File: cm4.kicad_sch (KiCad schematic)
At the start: 54 parts, among them Q1 MMBT2222AM3T5G, U3 PCA9671BS,118, U4 SN74LVC1G04DRY, U5 SN74LVC1G07DRY

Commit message: footprint assignment
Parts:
- R26, R27, R28, R29: renamed from R?; footprint (none) -> Resistor_SMD:R_0402_1005Metric
- gave numbers to parts that had none: 5
- renumbered R8 to R10, R9 to R11, R10 to R12, R11 to R13, R12 to R14, R13 to R15, R14 to R16, R15 to R17, R16 to R18, R17 to R19, R18 to R20, R19 to R21, R20 to R22, R21 to R23, R22 to R24, R23 to R25, R7 to R9
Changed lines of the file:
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@@
   (symbol (lib_id "Device:R_Small") (at 499.11 342.9 90) (unit 1)
     (in_bom yes) (on_board yes)
-    (property "Reference" "R15" (id 0) (at 496.57 341.63 90)
+    (property "Reference" "R17" (id 0) (at 496.57 341.63 90)
       (effects (font (size 1.27 1.27)) (justify left))
     )
@@
   (symbol (lib_id "Device:R_Small") (at 647.7 118.11 90) (unit 1)
     (in_bom yes) (on_board yes)
-    (property "Reference" "R?" (id 0) (at 645.16 116.84 90)
+    (property "Reference" "R29" (id 0) (at 645.16 116.84 90)
       (effects (font (size 1.27 1.27)) (justify left))
     )
@@
       (effects (font (size 1.27 1.27)) (justify right))
     )
-    (property "Footprint" "" (id 2) (at 647.7 118.11 0)
+    (property "Footprint" "Resistor_SMD:R_0402_1005Metric" (id 2) (at 647.7 118.11 0)
       (effects (font (size 1.27 1.27)) hide)
     )
@@
   (symbol (lib_id "Device:R_Small") (at 458.47 129.54 90) (unit 1)
     (in_bom yes) (on_board yes)
-    (property "Reference" "R9" (id 0) (at 453.39 128.27 90))
+    (property "Reference" "R11" (id 0) (at 453.39 128.27 90))
     (property "Value" "1k" (id 1) (at 463.55 128.27 90))
     (property "Footprint" "Resistor_SMD:R_0402_1005Metric" (id 2) (at 458.47 129.54 0)
@@
   (symbol (lib_id "Device:R_Small") (at 499.11 322.58 270) (mirror x) (unit 1)
     (in_bom yes) (on_board yes)
-    (property "Reference" "R13" (id 0) (at 496.57 321.31 90)
+    (property "Reference" "R15" (id 0) (at 496.57 321.31 90)
       (effects (font (size 1.27 1.27)) (justify right))
     )
@@
   (symbol (lib_id "Device:C_Small") (at 607.06 69.85 0) (unit 1)
     (in_bom yes) (on_board yes)
-    (property "Reference" "C?" (id 0) (at 608.965 68.58 0)
+    (property "Reference" "C9" (id 0) (at 608.965 68.58 0)
       (effects (font (size 1.27 1.27)) (justify left))
     )
@@
   (symbol (lib_id "Interface_I2C_NXP:PCA9641BSHP") (at 623.57 62.23 0) (unit 1)
     (in_bom yes) (on_board yes) (fields_autoplaced)
-    (property "Reference" "U?" (id 0) (at 670.56 53.34 0))
+    (property "Reference" "U6" (id 0) (at 670.56 53.34 0))
     (property "Value" "PCA9641BSHP" (id 1) (at 670.56 55.88 0))
     (property "Footprint" "Interface_I2C_NXP:SOT758-1_HVQFN-16_3x3mm_P0.5mm_EP1.75x1.75mm_NXP" (id 2) (at 670.56 142.24 0)
@@
   (symbol (lib_id "Device:R_Small") (at 500.38 97.79 180) (unit 1)
     (in_bom yes) (on_board yes)
-    (property "Reference" "R17" (id 0) (at 501.65 96.52 0)
+    (property "Reference" "R19" (id 0) (at 501.65 96.52 0)
       (effects (font (size 1.27 1.27)) (justify right))
     )
@@
   (symbol (lib_id "Device:R_Small") (at 414.02 383.54 270) (mirror x) (unit 1)
     (in_bom yes) (on_board yes)
-    (property "Reference" "R?" (id 0) (at 414.02 379.095 90))
+    (property "Reference" "R8" (id 0) (at 414.02 379.095 90))
     (property "Value" "5.1k" (id 1) (at 414.02 381 90))
     (property "Footprint" "Resistor_SMD:R_0402_1005Metric" (id 2) (at 414.02 383.54 0)
@@
   (symbol (lib_id "Device:R_Small") (at 554.99 203.2 90) (unit 1)
     (in_bom yes) (on_board yes)
-    (property "Reference" "R23" (id 0) (at 557.53 201.93 90)
+    (property "Reference" "R25" (id 0) (at 557.53 201.93 90)
       (effects (font (size 1.27 1.27)) (justify right))
     )
@@
   (symbol (lib_id "Device:R_Small") (at 647.7 110.49 90) (unit 1)
     (in_bom yes) (on_board yes)
-    (property "Reference" "R?" (id 0) (at 645.16 109.22 90)
+    (property "Reference" "R26" (id 0) (at 645.16 109.22 90)
       (effects (font (size 1.27 1.27)) (justify left))
     )
@@
       (effects (font (size 1.27 1.27)) (justify right))
     )
-    (property "Footprint" "" (id 2) (at 647.7 110.49 0)
+    (property "Footprint" "Resistor_SMD:R_0402_1005Metric" (id 2) (at 647.7 110.49 0)
       (effects (font (size 1.27 1.27)) hide)
     )
@@
   (symbol (lib_id "Device:R_Small") (at 504.19 191.77 0) (unit 1)
     (in_bom yes) (on_board yes)
-    (property "Reference" "R18" (id 0) (at 505.46 190.5 0)
+    (property "Reference" "R20" (id 0) (at 505.46 190.5 0)
       (effects (font (size 1.27 1.27)) (justify left))
     )
@@
   (symbol (lib_id "power:GND") (at 626.11 140.97 0) (unit 1)
     (in_bom yes) (on_board yes) (fields_autoplaced)
-    (property "Reference" "#PWR?" (id 0) (at 626.11 147.32 0)
+    (property "Reference" "#PWR016" (id 0) (at 626.11 147.32 0)
       (effects (font (size 1.27 1.27)) hide)
     )
@@
   (symbol (lib_id "Device:C_Small") (at 619.76 69.85 0) (unit 1)
     (in_bom yes) (on_board yes)
-    (property "Reference" "C?" (id 0) (at 621.665 68.58 0)
+    (property "Reference" "C10" (id 0) (at 621.665 68.58 0)
       (effects (font (size 1.27 1.27)) (justify left))
     )
@@
   (symbol (lib_id "Device:R_Small") (at 458.47 124.46 90) (unit 1)
     (in_bom yes) (on_board yes)
-    (property "Reference" "R7" (id 0) (at 453.39 123.19 90))
+    (property "Reference" "R9" (id 0) (at 453.39 123.19 90))
     (property "Value" "1k" (id 1) (at 463.55 123.19 90))
     (property "Footprint" "Resistor_SMD:R_0402_1005Metric" (id 2) (at 458.47 124.46 0)
@@
   (symbol (lib_id "Device:R_Small") (at 491.49 217.17 90) (unit 1)
     (in_bom yes) (on_board yes)
-    (property "Reference" "R11" (id 0) (at 491.49 212.09 90))
+    (property "Reference" "R13" (id 0) (at 491.49 212.09 90))
     (property "Value" "5.9k" (id 1) (at 491.49 214.63 90))
     (property "Footprint" "Resistor_SMD:R_0402_1005Metric" (id 2) (at 491.49 217.17 0)
@@
   (symbol (lib_id "Device:R_Small") (at 506.73 97.79 180) (unit 1)
     (in_bom yes) (on_board yes)
-    (property "Reference" "R19" (id 0) (at 508 96.52 0)
+    (property "Reference" "R21" (id 0) (at 508 96.52 0)
       (effects (font (size 1.27 1.27)) (justify right))
     )
@@
   (symbol (lib_id "Device:R_Small") (at 510.54 256.54 270) (mirror x) (unit 1)
     (in_bom yes) (on_board yes)
-    (property "Reference" "R20" (id 0) (at 508 255.27 90)
+    (property "Reference" "R22" (id 0) (at 508 255.27 90)
       (effects (font (size 1.27 1.27)) (justify right))
     )
@@
   (symbol (lib_id "Device:R_Small") (at 647.7 115.57 90) (unit 1)
     (in_bom yes) (on_board yes)
-    (property "Reference" "R?" (id 0) (at 645.16 114.3 90)
+    (property "Reference" "R28" (id 0) (at 645.16 114.3 90)
       (effects (font (size 1.27 1.27)) (justify left))
     )
@@
       (effects (font (size 1.27 1.27)) (justify right))
     )
-    (property "Footprint" "" (id 2) (at 647.7 115.57 0)
+    (property "Footprint" "Resistor_SMD:R_0402_1005Metric" (id 2) (at 647.7 115.57 0)
       (effects (font (size 1.27 1.27)) hide)
     )
@@
   (symbol (lib_id "power:GND") (at 619.76 80.01 0) (unit 1)
     (in_bom yes) (on_board yes) (fields_autoplaced)
-    (property "Reference" "#PWR?" (id 0) (at 619.76 86.36 0)
+    (property "Reference" "#PWR015" (id 0) (at 619.76 86.36 0)
       (effects (font (size 1.27 1.27)) hide)
     )
@@
   (symbol (lib_id "Device:R_Small") (at 499.11 353.06 90) (unit 1)
     (in_bom yes) (on_board yes)
-    (property "Reference" "R16" (id 0) (at 496.57 351.79 90)
+    (property "Reference" "R18" (id 0) (at 496.57 351.79 90)
       (effects (font (size 1.27 1.27)) (justify left))
     )
@@
   (symbol (lib_id "Device:R_Small") (at 414.02 375.92 270) (mirror x) (unit 1)
     (in_bom yes) (on_board yes)
-    (property "Reference" "R?" (id 0) (at 414.02 371.475 90))
+    (property "Reference" "R7" (id 0) (at 414.02 371.475 90))
     (property "Value" "5.1k" (id 1) (at 414.02 373.38 90))
     (property "Footprint" "Resistor_SMD:R_0402_1005Metric" (id 2) (at 414.02 375.92 0)
@@
   (symbol (lib_id "Device:R_Small") (at 554.99 199.39 90) (unit 1)
     (in_bom yes) (on_board yes)
-    (property "Reference" "R22" (id 0) (at 557.53 198.12 90)
+    (property "Reference" "R24" (id 0) (at 557.53 198.12 90)
       (effects (font (size 1.27 1.27)) (justify right))
     )
@@
   (symbol (lib_id "Device:R_Small") (at 499.11 332.74 90) (unit 1)
     (in_bom yes) (on_board yes)
-    (property "Reference" "R14" (id 0) (at 496.57 331.47 90)
+    (property "Reference" "R16" (id 0) (at 496.57 331.47 90)
       (effects (font (size 1.27 1.27)) (justify left))
     )
@@
   (symbol (lib_id "Device:R_Small") (at 480.06 224.79 0) (unit 1)
     (in_bom yes) (on_board yes)
-    (property "Reference" "R10" (id 0) (at 481.33 223.52 0)
+    (property "Reference" "R12" (id 0) (at 481.33 223.52 0)
       (effects (font (size 1.27 1.27)) (justify left))
     )
@@
   (symbol (lib_id "Device:R_Small") (at 647.7 113.03 90) (unit 1)
     (in_bom yes) (on_board yes)
-    (property "Reference" "R?" (id 0) (at 645.16 111.76 90)
+    (property "Reference" "R27" (id 0) (at 645.16 111.76 90)
       (effects (font (size 1.27 1.27)) (justify left))
     )
@@
       (effects (font (size 1.27 1.27)) (justify right))
     )
-    (property "Footprint" "" (id 2) (at 647.7 113.03 0)
+    (property "Footprint" "Resistor_SMD:R_0402_1005Metric" (id 2) (at 647.7 113.03 0)
       (effects (font (size 1.27 1.27)) hide)
     )
@@
   (symbol (lib_id "Device:R_Small") (at 513.08 97.79 180) (unit 1)
     (in_bom yes) (on_board yes)
-    (property "Reference" "R21" (id 0) (at 514.35 96.52 0)
+    (property "Reference" "R23" (id 0) (at 514.35 96.52 0)
       (effects (font (size 1.27 1.27)) (justify right))
     )
@@
   (symbol (lib_id "Device:R_Small") (at 458.47 127 90) (unit 1)
     (in_bom yes) (on_board yes)
-    (property "Reference" "R8" (id 0) (at 453.39 125.73 90))
+    (property "Reference" "R10" (id 0) (at 453.39 125.73 90))
     (property "Value" "1k" (id 1) (at 463.55 125.73 90))
     (property "Footprint" "Resistor_SMD:R_0402_1005Metric" (id 2) (at 458.47 127 0)
@@
   (symbol (lib_id "Device:R_Small") (at 499.11 298.45 270) (mirror x) (unit 1)
     (in_bom yes) (on_board yes)
-    (property "Reference" "R12" (id 0) (at 496.57 297.18 90)
-      (effects (font (size 1.27 1.27)) (justify right))
-    )
+    (property "Reference" "R14" (id 0) (at 496.57 297.18 90)
+      (effects (font (size 1.27 1.27)) (justify right))
+    )

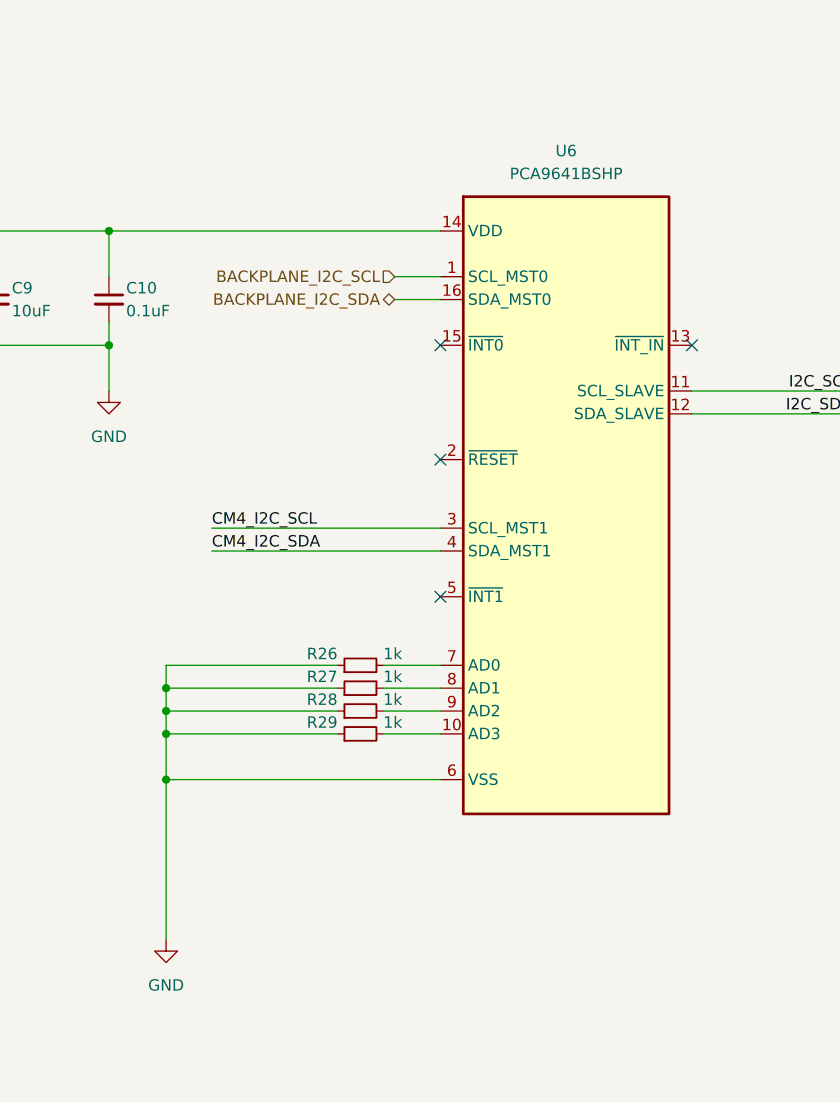
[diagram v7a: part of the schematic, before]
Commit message: symbol bug fix
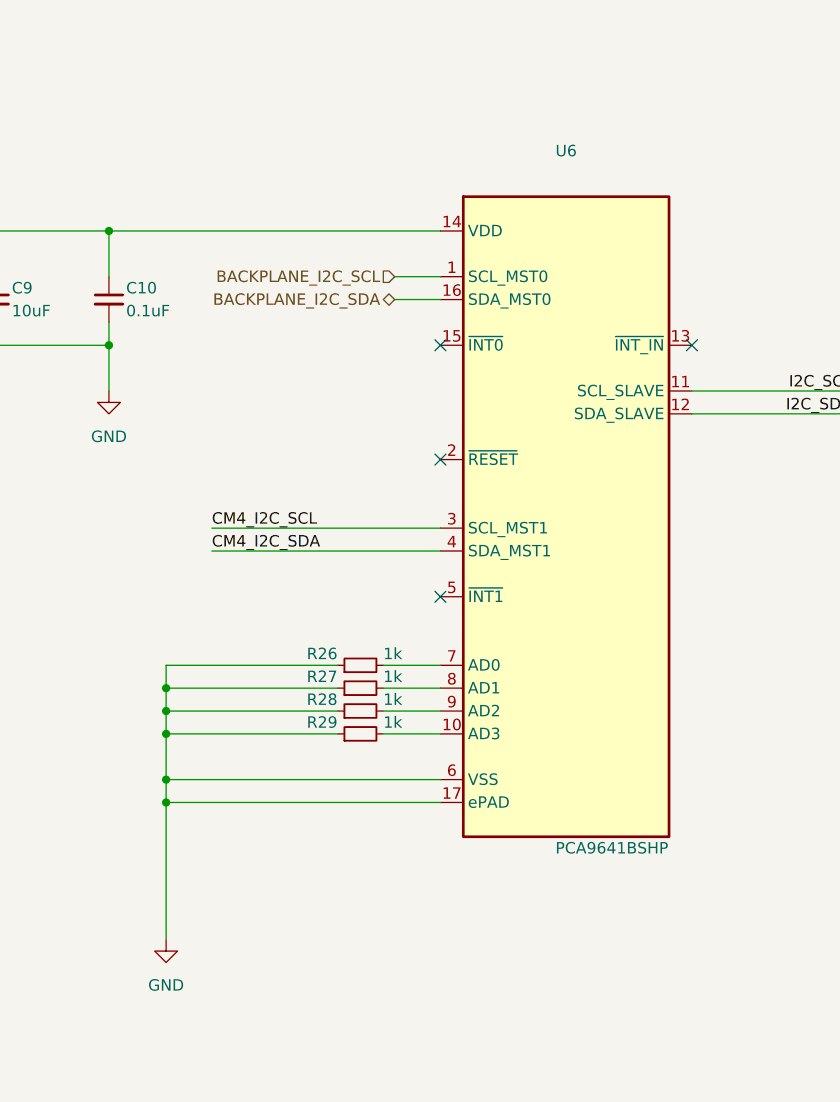
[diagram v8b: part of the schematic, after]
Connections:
- net GND: now also U6.17 (ePAD)
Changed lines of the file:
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@@
   (junction (at 506.73 107.95) (diameter 0) (color 0 0 0 0)
+  )
+  (junction (at 626.11 125.73) (diameter 0) (color 0 0 0 0)
   )
   (junction (at 504.19 185.42) (diameter 0) (color 0 0 0 0)
@@
     (stroke (width 0) (type default) (color 0 0 0 0))
   )
+  (wire (pts (xy 656.59 125.73) (xy 626.11 125.73))
+    (stroke (width 0) (type default) (color 0 0 0 0))
+  )
   (wire (pts (xy 281.94 381) (xy 256.54 381))
     (stroke (width 0) (type default) (color 0 0 0 0))
@@
     (stroke (width 0) (type default) (color 0 0 0 0))
   )
-  (wire (pts (xy 626.11 123.19) (xy 626.11 140.97))
+  (wire (pts (xy 626.11 123.19) (xy 626.11 125.73))
     (stroke (width 0) (type default) (color 0 0 0 0))
   )
@@
   (wire (pts (xy 513.08 332.74) (xy 501.65 332.74))
     (stroke (width 0) (type solid) (color 0 0 0 0))
+  )
+  (wire (pts (xy 626.11 125.73) (xy 626.11 140.97))
+    (stroke (width 0) (type default) (color 0 0 0 0))
   )
   (wire (pts (xy 142.24 353.06) (xy 162.56 353.06))
@@
     (in_bom yes) (on_board yes) (fields_autoplaced)
     (property "Reference" "U6" (id 0) (at 670.56 53.34 0))
-    (property "Value" "PCA9641BSHP" (id 1) (at 670.56 55.88 0))
+    (property "Value" "PCA9641BSHP" (id 1) (at 675.64 130.81 0))
     (property "Footprint" "Interface_I2C_NXP:SOT758-1_HVQFN-16_3x3mm_P0.5mm_EP1.75x1.75mm_NXP" (id 2) (at 670.56 142.24 0)
       (effects (font (size 1.27 1.27)) hide)
@@
     (pin "15")
     (pin "16")
+    (pin "17")
     (pin "2")
     (pin "3")
